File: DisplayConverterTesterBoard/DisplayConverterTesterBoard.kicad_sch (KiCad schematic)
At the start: 0 parts

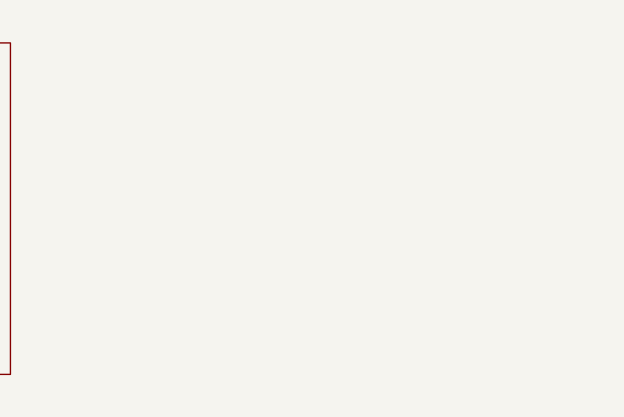
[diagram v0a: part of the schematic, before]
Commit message: added JDI 1.282in Memory LCD blank sch
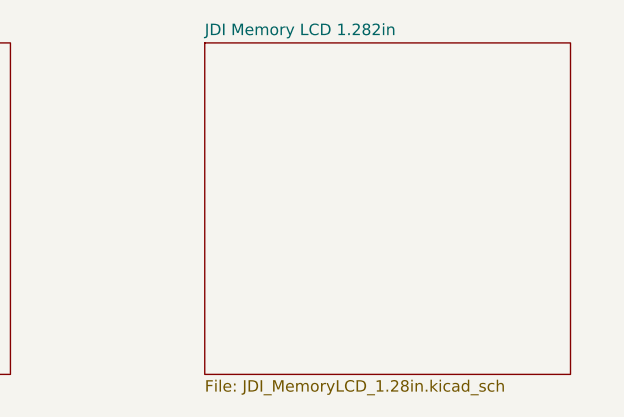
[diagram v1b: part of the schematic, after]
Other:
- added sheet JDI Memory LCD 1.282in (JDI_MemoryLCD_1.28in.kicad_sch)
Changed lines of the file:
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@@
 (kicad_sch (version 20230121) (generator eeschema)
   (paper "A4")
+  (sheet (at 186.69 50.8) (size 40.64 36.83) (fields_autoplaced)
+    (stroke (width 0.1524) (type solid))
+    (fill (color 0 0 0 0.0000))
+    (property "Sheetname" "JDI Memory LCD 1.282in" (at 186.69 50.0884 0)
+      (effects (font (size 1.27 1.27)) (justify left bottom))
+    )
+    (property "Sheetfile" "JDI_MemoryLCD_1.28in.kicad_sch" (at 186.69 88.2146 0)
+      (effects (font (size 1.27 1.27)) (justify left top))
+    )
+    (instances
+      (project "DisplayConverterTesterBoard"
+        (path "/58d9d6aa-d5e3-4b7b-b546-d57c329de758" (page "4"))
+      )
+    )
+  )
   (sheet (at 53.34 50.8) (size 45.72 36.83) (fields_autoplaced)
     (stroke (width 0.1524) (type solid))

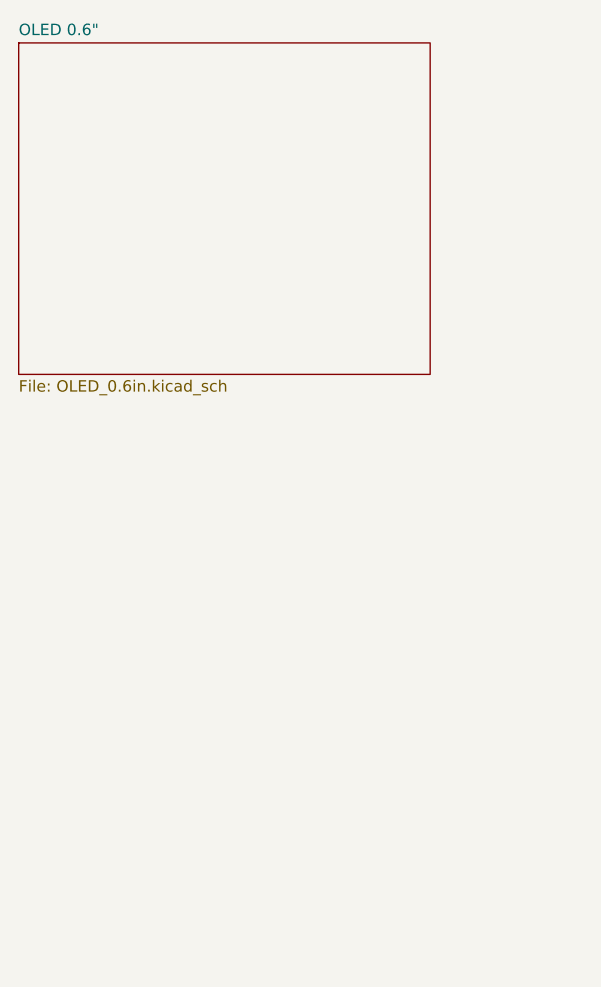
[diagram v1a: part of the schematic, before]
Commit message: moved MCU connector out to ROOT
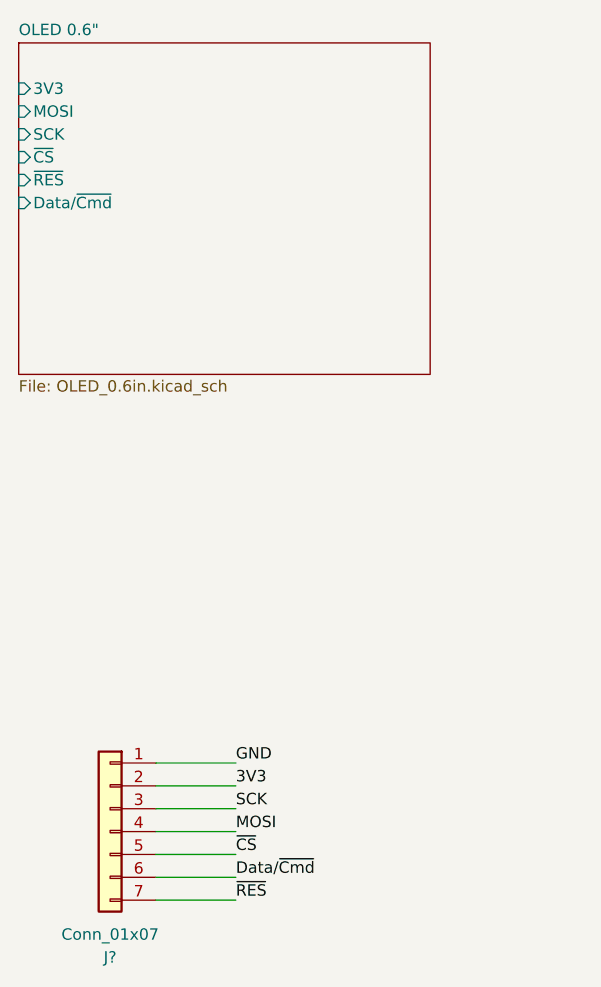
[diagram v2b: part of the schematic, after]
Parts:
- added J?: Conn_01x07, Connector_PinHeader_2.54mm:PinHeader_1x07_P2.54mm_Vertical, symbol Connector_Generic:Conn_01x07
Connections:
- new net 3V3: J?.2 (Pin_2)
- new net Data/~{Cmd}: J?.6 (Pin_6)
- new net GND: J?.1 (Pin_1)
- new net MOSI: J?.4 (Pin_4)
- new net SCK: J?.3 (Pin_3)
- new net ~{CS}: J?.5 (Pin_5)
- new net ~{RES}: J?.7 (Pin_7)
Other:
- sheet OLED 0.6" ports: added 3V3, Data/~{Cmd}, MOSI, SCK, ~{CS}, ~{RES}; removed none
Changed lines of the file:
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@@
 (kicad_sch (version 20230121) (generator eeschema)
   (paper "A4")
+  (wire (pts (xy 68.58 138.43) (xy 77.47 138.43))
+    (stroke (width 0) (type default))
+  )
+  (wire (pts (xy 68.58 133.35) (xy 77.47 133.35))
+    (stroke (width 0) (type default))
+  )
+  (wire (pts (xy 68.58 130.81) (xy 77.47 130.81))
+    (stroke (width 0) (type default))
+  )
+  (wire (pts (xy 68.58 143.51) (xy 77.47 143.51))
+    (stroke (width 0) (type default))
+  )
+  (wire (pts (xy 68.58 135.89) (xy 77.47 135.89))
+    (stroke (width 0) (type default))
+  )
+  (wire (pts (xy 68.58 146.05) (xy 77.47 146.05))
+    (stroke (width 0) (type default))
+  )
+  (wire (pts (xy 68.58 140.97) (xy 77.47 140.97))
+    (stroke (width 0) (type default))
+  )
+  (label "SCK" (at 77.47 135.89 0) (fields_autoplaced)
+    (effects (font (size 1.27 1.27)) (justify left bottom))
+  )
+  (label "MOSI" (at 77.47 138.43 0) (fields_autoplaced)
+    (effects (font (size 1.27 1.27)) (justify left bottom))
+  )
+  (label "Data{slash}~{Cmd}" (at 77.47 143.51 0) (fields_autoplaced)
+    (effects (font (size 1.27 1.27)) (justify left bottom))
+  )
+  (label "~{CS}" (at 77.47 140.97 0) (fields_autoplaced)
+    (effects (font (size 1.27 1.27)) (justify left bottom))
+  )
+  (label "3V3" (at 77.47 133.35 0) (fields_autoplaced)
+    (effects (font (size 1.27 1.27)) (justify left bottom))
+  )
+  (label "GND" (at 77.47 130.81 0) (fields_autoplaced)
+    (effects (font (size 1.27 1.27)) (justify left bottom))
+  )
+  (label "~{RES}" (at 77.47 146.05 0) (fields_autoplaced)
+    (effects (font (size 1.27 1.27)) (justify left bottom))
+  )
+  (symbol (lib_id "Connector_Generic:Conn_01x07") (at 63.5 138.43 0) (mirror y) (unit 1)
+    (in_bom yes) (on_board yes) (dnp no)
+    (property "Reference" "J?" (at 63.5 152.4 0)
+      (effects (font (size 1.27 1.27)))
+    )
+    (property "Value" "Conn_01x07" (at 63.5 149.86 0)
+      (effects (font (size 1.27 1.27)))
+    )
+    (property "Footprint" "Connector_PinHeader_2.54mm:PinHeader_1x07_P2.54mm_Vertical" (at 63.5 138.43 0)
+      (effects (font (size 1.27 1.27)) hide)
+    )
+    (property "Datasheet" "~" (at 63.5 138.43 0)
+      (effects (font (size 1.27 1.27)) hide)
+    )
+    (pin "1")
+    (pin "2")
+    (pin "3")
+    (pin "4")
+    (pin "5")
+    (pin "6")
+    (pin "7")
+    (instances
+      (project "DisplayConverterTesterBoard"
+        (path "/58d9d6aa-d5e3-4b7b-b546-d57c329de758/7553e832-beab-499d-896a-2d765e7d0d57"
+          (reference "J?") (unit 1)
+        )
+        (path "/58d9d6aa-d5e3-4b7b-b546-d57c329de758"
+          (reference "J?") (unit 1)
+        )
+      )
+    )
+  )
   (sheet (at 186.69 50.8) (size 40.64 36.83) (fields_autoplaced)
     (stroke (width 0.1524) (type solid))
@@
       (effects (font (size 1.27 1.27)) (justify left top))
     )
+    (pin "3V3" input (at 53.34 55.88 180)
+      (effects (font (size 1.27 1.27)) (justify left))
+    )
+    (pin "MOSI" input (at 53.34 58.42 180)
+      (effects (font (size 1.27 1.27)) (justify left))
+    )
+    (pin "SCK" input (at 53.34 60.96 180)
+      (effects (font (size 1.27 1.27)) (justify left))
+    )
+    (pin "~{CS}" input (at 53.34 63.5 180)
+      (effects (font (size 1.27 1.27)) (justify left))
+    )
+    (pin "~{RES}" input (at 53.34 66.04 180)
+      (effects (font (size 1.27 1.27)) (justify left))
+    )
+    (pin "Data{slash}~{Cmd}" input (at 53.34 68.58 180)
+      (effects (font (size 1.27 1.27)) (justify left))
+    )
     (instances
